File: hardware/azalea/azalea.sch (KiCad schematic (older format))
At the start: 86 parts, among them J1 NEIGHBOR1, J2 NEIGHBOR2, J3 USB-MICRO-B-SHIELDED, J4 USB-MICRO-B-SHIELDED, J5 JTAG, J6 CONN_02X03, J7 BONUS_ROW, SW1 DFU, SW2 RESET, U1 LPC4330FBD144, U2 W25Q16DV, U3 AP7333, U4 IP4220CZ6, U5 NX5P2553GV, X1 XTAL4PIN, X2 RTC_XTAL

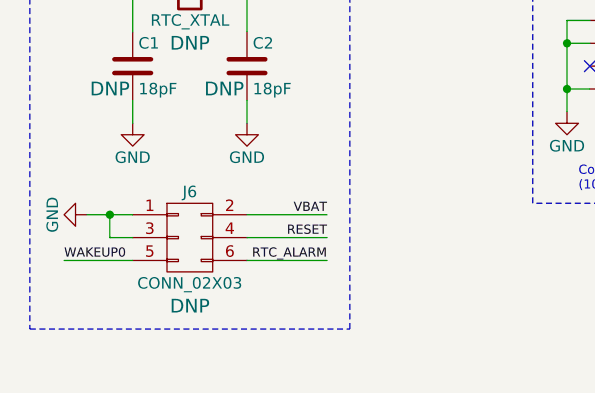
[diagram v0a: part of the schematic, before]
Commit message: azalea: renamed RTC header
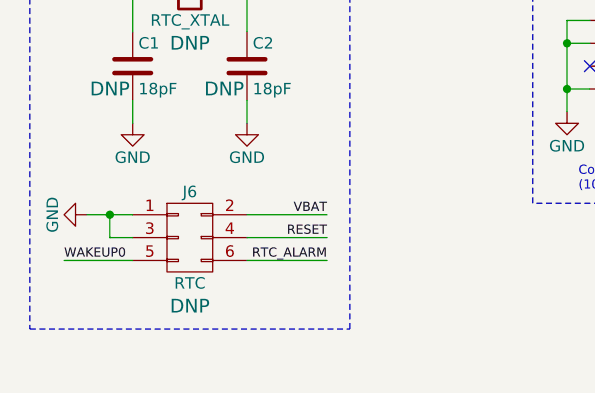
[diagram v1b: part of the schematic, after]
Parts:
- J6: value CONN_02X03 -> RTC
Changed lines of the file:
@@
 P 1750 9650
 F 0 "J6" H 1750 9850 50  0000 C CNN
-F 1 "CONN_02X03" H 1750 9450 50  0000 C CNN
+F 1 "RTC" H 1750 9450 50  0000 C CNN
 F 2 "" H 1750 8450 60  0000 C CNN
 F 3 "" H 1750 8450 60  0000 C CNN

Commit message: azalea: module assignments
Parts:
- C1, C10, C11, C12, C13, C14, C15, C16, C17, C18, C19, C2, C20, C21, C22, C23, C24, C25, C3, C4, C5, C6, C7, C8, C9, FB1, FB2, FB3, R1, R10, R11, R12, R13, R14, R15, R16, R17, R18, R19, R2, R20, R21, R22, R23, R24, R3, R4, R5, R6, R7, R8, R9: footprint (none) -> gsg-modules:0603
- D1, D2, D3, D4: footprint (none) -> gsg-modules:0603D
- J1, J2: footprint (none) -> gsg-modules:HEADER-2x20
- J3, J4: footprint (none) -> gsg-modules:USB-MICROB-FCI-10103592-EXT
- J5: footprint (none) -> gsg-modules:50MIL-HEADER-2x5-TH
- J6: footprint (none) -> gsg-modules:HEADER-2x3
- J7: footprint (none) -> gsg-modules:HEADER-1x20
- SW1, SW2: footprint (none) -> gsg-modules:SWITCH-FSMRA
- TP1, TP10, TP11, TP12, TP13, TP14, TP2, TP3, TP4, TP5, TP6, TP7, TP8, TP9: footprint (none) -> gsg-modules:TESTPOINT-50MIL
- U1: footprint (none) -> gsg-modules:LQFP144
- U2: footprint (none) -> gsg-modules:SOIC8-208
- U3: footprint (none) -> gsg-modules:SOT23-3
- U4, U5: footprint (none) -> gsg-modules:SOT457
- X1: footprint (none) -> gsg-modules:XTAL3.2x2.5mm
- X2: footprint (none) -> gsg-modules:XTAL-AB26TRQ

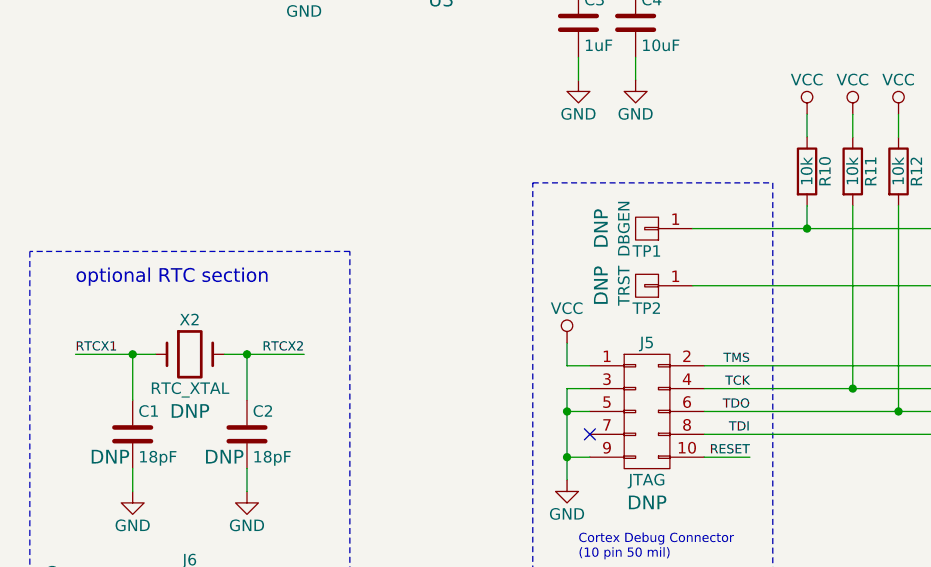
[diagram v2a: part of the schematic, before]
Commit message: azalea: reversed RTC XTAL connections
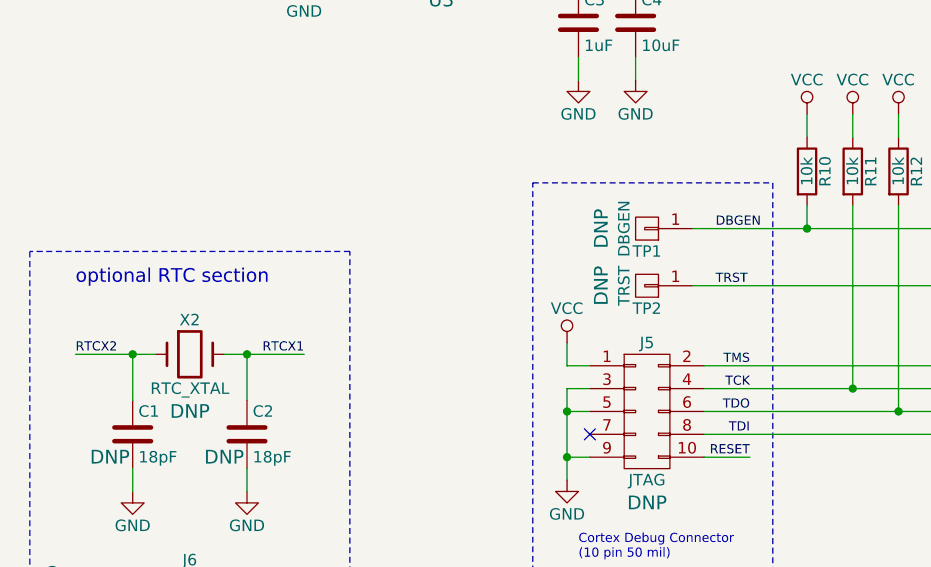
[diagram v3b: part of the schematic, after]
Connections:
- net RTCX1: now also C2.1, X2.2; no longer C1.1, X2.1
- net RTCX2: now also C1.1, X2.1; no longer C2.1, X2.2
- net DBGEN: now reaches R10.2, TP1.1 (P1), U1.28 (DBGEN)
- net TRST: now reaches TP2.1 (P1), U1.29 (TRST)
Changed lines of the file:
@@
 	0    1    1    0
 $EndComp
+Text Label 1250 8550 0    40   ~ 0
+RTCX2
 Text Label 2250 8550 2    40   ~ 0
-RTCX2
-Text Label 1250 8550 0    40   ~ 0
 RTCX1
 Text Label 8300 2300 3    40   ~ 0
@@
 Text Notes 3450 9450 0    40   ~ 0
 Cortex Debug Connector\n(10 pin 50 mil)
+Text Label 4050 8000 0    40   ~ 0
+DBGEN
+Text Label 4050 8250 0    40   ~ 0
+TRST
 $EndSCHEMATC

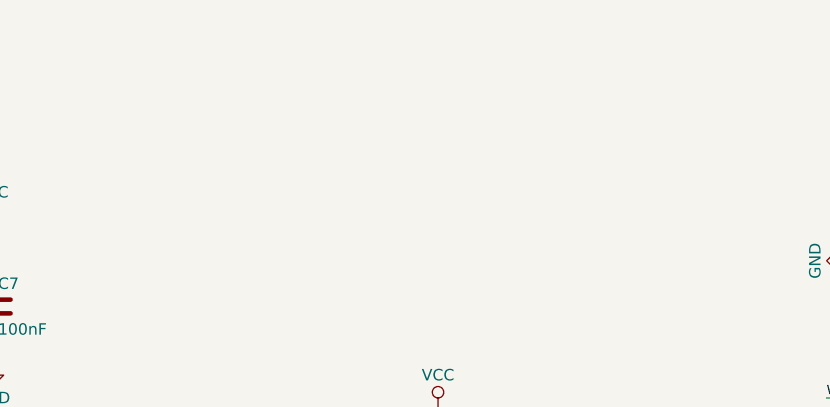
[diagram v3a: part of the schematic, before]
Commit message: azalea: added mounting holes
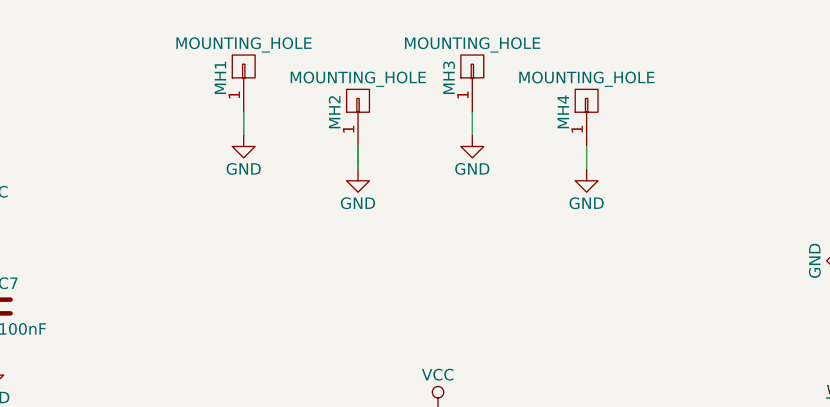
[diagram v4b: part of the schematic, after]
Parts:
- added MH1, MH2, MH3, MH4: MOUNTING_HOLE, gsg-modules:HOLE126MIL-COPPER, symbol CONN_01X01
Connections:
- net GND: now also MH1.1 (P1), MH2.1 (P1), MH3.1 (P1), MH4.1 (P1)
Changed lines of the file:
@@
 Text Label 4050 8250 0    40   ~ 0
 TRST
+$Comp
+L CONN_01X01 MH3
+U 1 1 5600EED5
+P 13650 850
+F 0 "MH3" H 13600 950 50  0000 C CNN
+F 1 "MOUNTING_HOLE" V 13750 850 50  0000 C CNN
+F 2 "gsg-modules:HOLE126MIL-COPPER" H 13650 850 60  0001 C CNN
+F 3 "" H 13650 850 60  0000 C CNN
+F 4 "DNP" H 13650 850 60  0001 C CNN "Note"
+	1    13650 850
+	0    -1   -1   0
+$EndComp
+$Comp
+L GND #PWR078
+U 1 1 5600F9D3
+P 13650 1150
+F 0 "#PWR078" H 13650 900 50  0001 C CNN
+F 1 "GND" H 13650 1000 50  0000 C CNN
+F 2 "" H 13650 1150 60  0000 C CNN
+F 3 "" H 13650 1150 60  0000 C CNN
+	1    13650 1150
+	1    0    0    -1
+$EndComp
+Wire Wire Line
+	13650 1050 13650 1150
+$Comp
+L CONN_01X01 MH4
+U 1 1 560100F3
+P 14150 1000
+F 0 "MH4" H 14100 1100 50  0000 C CNN
+F 1 "MOUNTING_HOLE" V 14250 1000 50  0000 C CNN
+F 2 "gsg-modules:HOLE126MIL-COPPER" H 14150 1000 60  0001 C CNN
+F 3 "" H 14150 1000 60  0000 C CNN
+F 4 "DNP" H 14150 1000 60  0001 C CNN "Note"
+	1    14150 1000
+	0    -1   -1   0
+$EndComp
+$Comp
+L GND #PWR079
+U 1 1 560100F9
+P 14150 1300
+F 0 "#PWR079" H 14150 1050 50  0001 C CNN
+F 1 "GND" H 14150 1150 50  0000 C CNN
+F 2 "" H 14150 1300 60  0000 C CNN
+F 3 "" H 14150 1300 60  0000 C CNN
+	1    14150 1300
+	1    0    0    -1
+$EndComp
+Wire Wire Line
+	14150 1200 14150 1300
+$Comp
+L CONN_01X01 MH1
+U 1 1 56010ADB
+P 12650 850
+F 0 "MH1" H 12600 950 50  0000 C CNN
+F 1 "MOUNTING_HOLE" V 12750 850 50  0000 C CNN
+F 2 "gsg-modules:HOLE126MIL-COPPER" H 12650 850 60  0001 C CNN
+F 3 "" H 12650 850 60  0000 C CNN
+F 4 "DNP" H 12650 850 60  0001 C CNN "Note"
+	1    12650 850
+	0    -1   -1   0
+$EndComp
+$Comp
+L GND #PWR080
+U 1 1 56010AE1
+P 12650 1150
+F 0 "#PWR080" H 12650 900 50  0001 C CNN
+F 1 "GND" H 12650 1000 50  0000 C CNN
+F 2 "" H 12650 1150 60  0000 C CNN
+F 3 "" H 12650 1150 60  0000 C CNN
+	1    12650 1150
+	1    0    0    -1
+$EndComp
+Wire Wire Line
+	12650 1050 12650 1150
+$Comp
+L CONN_01X01 MH2
+U 1 1 56010AE9
+P 13150 1000
+F 0 "MH2" H 13100 1100 50  0000 C CNN
+F 1 "MOUNTING_HOLE" V 13250 1000 50  0000 C CNN
+F 2 "gsg-modules:HOLE126MIL-COPPER" H 13150 1000 60  0001 C CNN
+F 3 "" H 13150 1000 60  0000 C CNN
+F 4 "DNP" H 13150 1000 60  0001 C CNN "Note"
+	1    13150 1000
+	0    -1   -1   0
+$EndComp
+$Comp
+L GND #PWR081
+U 1 1 56010AEF
+P 13150 1300
+F 0 "#PWR081" H 13150 1050 50  0001 C CNN
+F 1 "GND" H 13150 1150 50  0000 C CNN
+F 2 "" H 13150 1300 60  0000 C CNN
+F 3 "" H 13150 1300 60  0000 C CNN
+	1    13150 1300
+	1    0    0    -1
+$EndComp
+Wire Wire Line
+	13150 1200 13150 1300
 $EndSCHEMATC

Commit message: azalea: selected lower profile switch
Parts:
- SW1, SW2: footprint gsg-modules:SWITCH-FSMRA -> gsg-modules:SWITCH-PTS840-P; Description (none) -> SWITCH TACTILE SPST-NO 0.05A 12V; Manufacturer (none) -> C&K Components; Part Number (none) -> PTS840 PM SMTR LFS
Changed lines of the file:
@@
 F 0 "SW2" H 1850 1560 50  0000 C CNN
 F 1 "RESET" H 1700 1370 50  0000 C CNN
-F 2 "gsg-modules:SWITCH-FSMRA" H 1700 1450 60  0001 C CNN
+F 2 "gsg-modules:SWITCH-PTS840-P" H 1700 1450 60  0001 C CNN
 F 3 "" H 1700 1450 60  0000 C CNN
+F 4 "C&K Components" H 1700 1450 60  0001 C CNN "Manufacturer"
+F 5 "PTS840 PM SMTR LFS" H 1700 1450 60  0001 C CNN "Part Number"
+F 6 "SWITCH TACTILE SPST-NO 0.05A 12V" H 1700 1450 60  0001 C CNN "Description"
 	1    1700 1450
 	1    0    0    -1
@@
 F 0 "SW1" H 3150 1560 50  0000 C CNN
 F 1 "DFU" H 3000 1370 50  0000 C CNN
-F 2 "gsg-modules:SWITCH-FSMRA" H 3000 1450 60  0001 C CNN
+F 2 "gsg-modules:SWITCH-PTS840-P" H 3000 1450 60  0001 C CNN
 F 3 "" H 3000 1450 60  0000 C CNN
+F 4 "C&K Components" H 3000 1450 60  0001 C CNN "Manufacturer"
+F 5 "PTS840 PM SMTR LFS" H 3000 1450 60  0001 C CNN "Part Number"
+F 6 "SWITCH TACTILE SPST-NO 0.05A 12V" H 3000 1450 60  0001 C CNN "Description"
 	1    3000 1450
 	1    0    0    -1

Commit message: azalea: completed most of the routing
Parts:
- removed J6: RTC, gsg-modules:HEADER-2x3, symbol CONN_02X03
- removed TP14: P2_9, gsg-modules:TESTPOINT-50MIL, symbol CONN_01X01
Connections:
- net ADC0_0: now also J2.5 (P5); no longer J2.10 (P10)
- net ADC0_2: now also J7.5 (P5); no longer J7.4 (P4)
- net ADC0_5: now also J7.4 (P4); no longer J7.3 (P3)
- net CLK2: now also J2.12 (P12); no longer J2.26 (P26)
- net GND: now also J7.10 (P10), J7.19 (P19)
- net LED1: now also U1.134 (P7_6); no longer U1.132 (P7_4)
- net LED2: now also U1.3 (P4_1); no longer U1.133 (P7_5)
- net LED3: now also U1.133 (P7_5); no longer U1.134 (P7_6)
- net LED4: now also U1.132 (P7_4); no longer U1.3 (P4_1)
- net P1_1: now also J1.10 (P10); no longer J1.9 (P9)
- net P1_19: now also J1.38 (P38); no longer J1.37 (P37)
- net P1_20: now also J1.37 (P37); no longer J1.38 (P38)
- net P1_3: now also J1.40 (P40); no longer J1.39 (P39)
- net P1_4: now also J1.39 (P39); no longer J1.40 (P40)
- net P2_1: now also J2.35 (P35); no longer J2.37 (P37)
- net P2_10: now also J7.14 (P14); no longer J7.12 (P12)
- net P2_11: now also J7.13 (P13); no longer J7.11 (P11)
- net P2_12: now also J7.7 (P7); no longer J7.10 (P10)
- net P2_13: now also J7.8 (P8); no longer J7.9 (P9)
- net P2_2: now also J2.33 (P33); no longer J2.35 (P35)
- net P2_3: now also J2.20 (P20); no longer J2.32 (P32)
- net P2_4: now also J2.19 (P19); no longer J2.31 (P31)
- net P2_5: now also J2.18 (P18); no longer J2.30 (P30)
- net P2_6: now also J2.15 (P15); no longer J2.29 (P29)
- net P2_7: now also J2.14 (P14); no longer J2.28 (P28)
- net P2_8: now also J2.13 (P13); no longer J2.27 (P27)
- net P2_9: now also J7.6 (P6); no longer J7.13 (P13)
- net P3_0: now also J2.26 (P26); no longer J2.24 (P24)
- net P3_1: now also J2.24 (P24); no longer J2.22 (P22)
- net P3_2: now also J2.22 (P22); no longer J2.20 (P20)
- net P3_3: now also J2.32 (P32); no longer J2.18 (P18)
- net P3_4: now also J2.28 (P28); no longer J2.17 (P17)
- net P3_5: now also J2.37 (P37); no longer J2.16 (P16)
- net P3_6: now also J2.38 (P38); no longer J2.15 (P15)
- net P3_7: now also J2.30 (P30); no longer J2.14 (P14)
- net P4_0: now also J2.4 (P4); no longer J2.11 (P11)
- net P4_6: now also J2.10 (P10); no longer J2.5 (P5)
- net P4_7: now also J2.11 (P11); no longer J2.4 (P4)
- net P5_1: now also J1.9 (P9); no longer J1.10 (P10)
- net P6_1: now also J7.18 (P18); no longer J7.19 (P19)
- net P6_10: now also J7.15 (P15); no longer J7.14 (P14)
- net P6_2: now also J7.17 (P17); no longer J7.18 (P18)
- net P6_3: now also J2.36 (P36); no longer J2.38 (P38)
- net P6_4: now also J7.2 (P2); no longer J7.17 (P17)
- net P6_5: now also J7.3 (P3); no longer J7.16 (P16)
- net P6_6: now also J2.34 (P34); no longer J2.36 (P36)
- net P6_7: now also J2.31 (P31); no longer J2.34 (P34)
- net P6_8: now also J2.29 (P29); no longer J2.33 (P33)
- net P6_9: now also J7.16 (P16); no longer J7.15 (P15)
- net P7_0: now also J2.27 (P27); no longer J2.25 (P25)
- net P7_1: now also J2.25 (P25); no longer J2.23 (P23)
- net P7_2: now also J2.23 (P23); no longer J2.21 (P21)
- net P7_7: now also J2.16 (P16); no longer J2.12 (P12)
- net PF_4: now also J2.21 (P21); no longer J2.19 (P19)
- net RESET: now also J7.11 (P11)
- net RTC_ALARM: now also J7.9 (P9)
- net VBAT: now also J7.12 (P12)
- net WAKEUP0: now also J2.17 (P17); no longer J2.13 (P13)
- net USB0_D-: now reaches J3.2 (D-), U1.20 (USB0_DM), U4.1 (ESD1), U4.6 (ESD4)
- net USB0_D+: now reaches J3.3 (D+), U1.18 (USB0_DP), U4.3 (ESD2), U4.4 (ESD3)
- net USB1_D+: now reaches C9.1, R20.2, U1.89 (USB1_DP)
- net USB1_D-: now reaches C8.1, R19.2, U1.90 (USB1_DM)
- net ADC0_1: no longer names the net of U1.2 (ADC0_1/ADC1_1)
- net ADC0_1: no longer J7.2 (P2)
- net ADC0_3: no longer names the net of U1.139 (ADC0_3/ADC1_3)
- net ADC0_3: no longer J7.6 (P6)
- net ADC0_4: no longer names the net of U1.138 (ADC0_4/ADC1_4)
- net ADC0_4: no longer J7.7 (P7)
- net ADC0_6: no longer names the net of U1.142 (ADC0_6/ADC1_6)
- net ADC0_6: no longer J7.5 (P5)
- net ADC0_7: no longer names the net of U1.136 (ADC0_7/ADC1_7)
- net ADC0_7: no longer J7.8 (P8)
- no-connect marks 1 -> 6

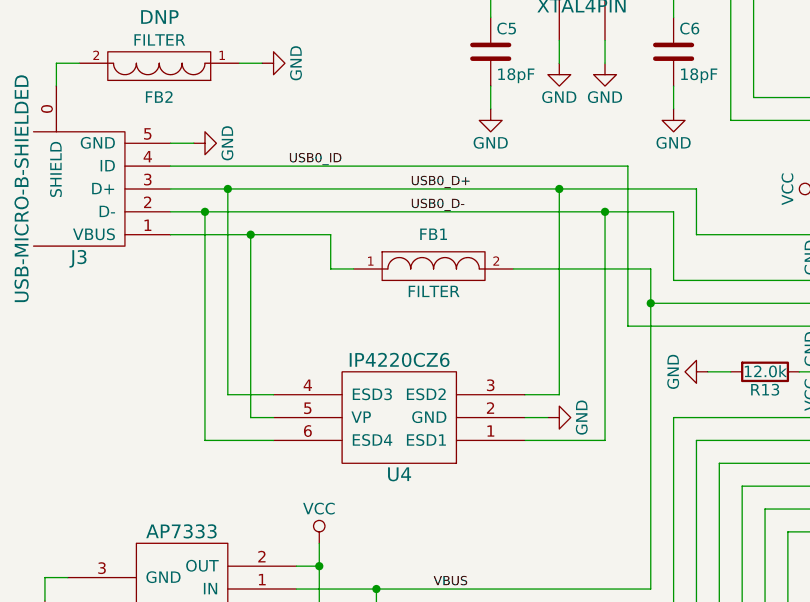
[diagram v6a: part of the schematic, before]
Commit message: azalea: reoriented ESD diode, added USB0_ID protection
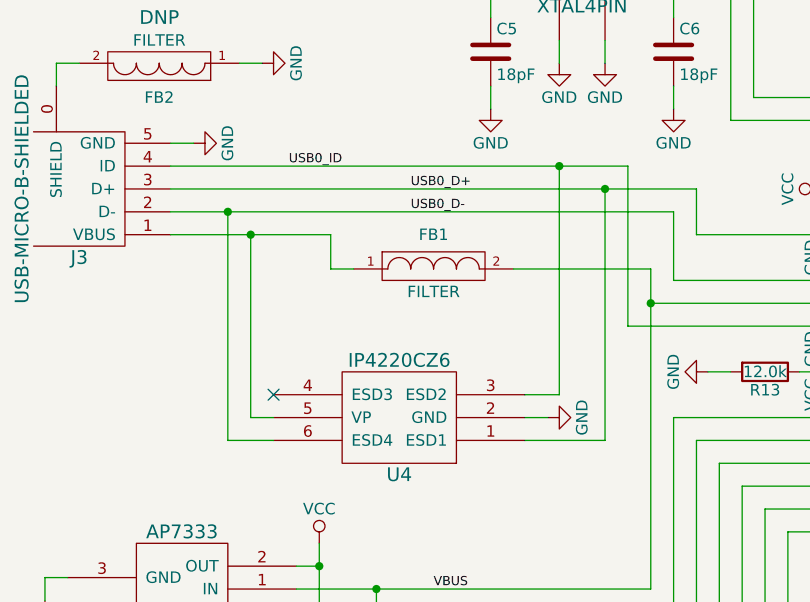
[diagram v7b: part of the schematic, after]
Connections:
- net USB0_D+: now also U4.1 (ESD1); no longer U4.3 (ESD2), U4.4 (ESD3)
- net USB0_D-: no longer U4.1 (ESD1)
- net USB0_ID: now also U4.3 (ESD2)
- no-connect marks 6 -> 7
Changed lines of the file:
@@
 	5000 5500 5000 5200
-Wire Wire Line
-	5000 5200 2800 5200
 Wire Wire Line
 	5750 5800 5850 5800
@@
 	5750 6000 5850 6000
 Wire Wire Line
-	3250 6000 3050 6000
-Wire Wire Line
-	3050 6000 3050 5100
-Connection ~ 3050 5100
-Wire Wire Line
-	3250 6200 2950 6200
-Wire Wire Line
-	2950 6200 2950 5200
-Connection ~ 2950 5200
-Wire Wire Line
 	2800 5300 3500 5300
 Wire Wire Line
@@
 	4350 6000 4500 6000
 Wire Wire Line
-	4500 6000 4500 5100
-Connection ~ 4500 5100
-Wire Wire Line
 	4350 6200 4700 6200
-Wire Wire Line
-	4700 6200 4700 5200
-Connection ~ 4700 5200
 Wire Wire Line
 	4350 6100 4450 6100
@@
 Text Label 11750 5500 0    40   ~ 0
 USB1_D+
+Wire Wire Line
+	5000 5200 2800 5200
+Connection ~ 3050 5200
+Wire Wire Line
+	4700 6200 4700 5100
+Connection ~ 4700 5100
+Wire Wire Line
+	4500 6000 4500 5000
+Connection ~ 4500 5000
+Wire Wire Line
+	3250 6200 3050 6200
+Wire Wire Line
+	3050 6200 3050 5200
+NoConn ~ 3250 6000
 $EndSCHEMATC
